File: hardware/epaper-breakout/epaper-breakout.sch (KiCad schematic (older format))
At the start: 94 parts, among them J1 XF2M-3315-1A, J2 C10418, J3 Conn_02x06_Counter_Clockwise, J4 ED060SC4, J5 Conn_01x01_Male, J6 Conn_01x01_Male, J7 Conn_01x10, Q1 AO3401A, Q3 MMBT3904, Q4 MMBT3904, U1 MCP1700-3302E_SOT23, U10 ED060SC7, U11 TP4056, U12 CH340C, U2 PCA9555PW, U3 TPS651851RSLR, U4 XC6206PxxxMR, U5 ESP32-WROVER, U6 ED060XC5

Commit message: re-assign footprints
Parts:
- added C34, C36: 1uF/50V, Capacitor_SMD:C_1206_3216Metric, symbol Device:C
- added C35, C37, C38: 1uF/25V, Capacitor_SMD:C_0805_2012Metric, symbol Device:C
- added R26, R27, R28, R29: 47k, Resistor_SMD:R_0805_2012Metric, symbol Device:R
- added R30: 100k, Resistor_SMD:R_0805_2012Metric, symbol Device:R
- added TP1: VCOM, TestPoint:TestPoint_Pad_2.0x2.0mm, symbol Connector:TestPoint
- C1, C11, C24, C26, C31, C5, C7, C8: footprint Capacitor_SMD:C_0603_1608Metric -> Capacitor_SMD:C_0805_2012Metric; LCSC C19702 -> C1779
- C10, C6: value 47uF -> 22uF; footprint Capacitor_SMD:C_0603_1608Metric -> Capacitor_SMD:C_0805_2012Metric; LCSC C19702 -> C45783
- C12, C32, C9: footprint Capacitor_SMD:C_0603_1608Metric -> Capacitor_SMD:C_0805_2012Metric; LCSC C19702 -> C15850
- C13, C14, C15, C16, C18, C19, C2, C21, C22, C23, C28, C3, C4: footprint Capacitor_SMD:C_0603_1608Metric -> Capacitor_SMD:C_0805_2012Metric
- C20, C25: footprint Capacitor_SMD:C_0603_1608Metric -> Capacitor_SMD:C_0805_2012Metric; LCSC C14858 -> C1710
- C27, C33: footprint Capacitor_SMD:C_0603_1608Metric -> Capacitor_SMD:C_0805_2012Metric; LCSC C19702 -> C49217
- C29, C30: footprint Capacitor_SMD:C_0603_1608Metric -> Capacitor_SMD:C_0805_2012Metric; LCSC C14858 -> C49678
- J4: LCSC C92280 -> C92280/ C262546
- J7: footprint (none) -> Connector_PinHeader_2.54mm:PinHeader_2x05_P2.54mm_Vertical
- L1: footprint Inductor_SMD:L_6.3x6.3_H3 -> Inductor_SMD:L_Taiyo-Yuden_NR-50xx_HandSoldering; LCSC C206321 -> C222947
- L2: footprint Inductor_SMD:L_6.3x6.3_H3 -> Inductor_SMD:L_Taiyo-Yuden_NR-40xx_HandSoldering; LCSC C206321 -> C92959
- R12, R5, R7: footprint (none) -> Resistor_SMD:R_0805_2012Metric; LCSC (none) -> C17477
- R17: value 1M -> 1k; LCSC C17616 -> C17513
- R18: footprint (none) -> Resistor_SMD:R_0805_2012Metric
- R20: LCSC C17593 -> C17740
- R24: LCSC C17593 -> C17713
- TH1: footprint (none) -> Resistor_SMD:R_0603_1608Metric; LCSC (none) -> C71448
- U2: LCSC (none) -> C128392
- U3: footprint RSL48_4P4X4P4 -> tps65185:TPS651851RSLR
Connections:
- net +22V: now also C34.1, R26.1
- net -15V: now also C35.1, R27.1
- net -20V: now also C36.1, R28.1
- net 15V: now also C37.1, R29.1
- net EP_VCOM: now also C38.1, R30.1, TP1.1
- net GND: now also C34.2, C35.2, C36.2, C37.2, C38.2, R26.2, R27.2, R28.2, R29.2, R30.2
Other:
- note added: "Close to EPD connector"
- moved on the sheet: C1, C10, C11, C12, C13, C14, C16, C19, C2, C20, C24, C25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

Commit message: pcb routing
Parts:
- removed J3: Conn_02x06_Counter_Clockwise, Connector_PinHeader_2.54mm:PinHeader_2x06_P2.54mm_Vertical, symbol Connector_Generic:Conn_02x06_Counter_Clockwise
- removed J7: Conn_01x10, Connector_PinHeader_2.54mm:PinHeader_2x05_P2.54mm_Vertical, symbol Connector_Generic:Conn_01x10
- removed R12, R7: 0, Resistor_SMD:R_0805_2012Metric, symbol Device:R
- removed R17: 1k, Resistor_SMD:R_0805_2012Metric, symbol Device:R
- removed U10: ED060SC7, epaper-breakout:AXT334124, symbol epd_breakout:ED060SC7
- added J3: Conn_02x05_Counter_Clockwise, Connector_PinHeader_2.54mm:PinHeader_2x05_P2.54mm_Vertical, symbol Connector_Generic:Conn_02x05_Counter_Clockwise
- added J7: Conn_01x12, Connector_PinHeader_2.54mm:PinHeader_2x06_P2.54mm_Vertical, symbol Connector_Generic:Conn_01x12
- R1, R10, R11, R13, R14, R15, R16, R18, R19, R2, R20, R21, R22, R23, R24, R25, R26, R27, R28, R29, R3, R30, R4, R5, R6, R8, R9: footprint Resistor_SMD:R_0805_2012Metric -> Resistor_SMD:R_0603_1608Metric
- TH1: value 100k -> 10k; LCSC C71448 -> C76589
- TP_VCOM1: renamed from TP1; footprint TestPoint:TestPoint_Pad_2.0x2.0mm -> TestPoint:TestPoint_Pad_D2.0mm
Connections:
- net +3.3V: now also J3.6 (Pin_6), J7.1 (Pin_1)
- net -20V: now also U3.29 (VEE_DIS)
- net A0: now also J3.3 (Pin_3)
- net BAT+: now also R21.1
- net GND: now also U2.2 (A1), U2.3 (A2), J3.5 (Pin_5), J7.2 (Pin_2)
- net IO0: now also J3.7 (Pin_7)
- net MISO: now also J3.10 (Pin_10)
- net MOSI: now also J3.8 (Pin_8)
- net SCL: now also J7.4 (Pin_4)
- net SCLK: now also J3.9 (Pin_9)
- net SDA: now also J7.3 (Pin_3)
- net SENSOR_VN: now also J3.2 (Pin_2)
- net SENSOR_VP: now also J3.1 (Pin_1)
- net SW_VIN: now also J3.4 (Pin_4); no longer R21.1
- net at U2.10 (IO0_6): now also J7.11 (Pin_11)
- net at U2.11 (IO0_7): now also J7.12 (Pin_12)
- net at U2.4 (IO0_0): now also J7.5 (Pin_5)
- net at U2.5 (IO0_1): now also J7.6 (Pin_6)
- net at U2.6 (IO0_2): now also J7.7 (Pin_7)
- net at U2.7 (IO0_3): now also J7.8 (Pin_8)
- net at U2.8 (IO0_4): now also J7.9 (Pin_9)
- net at U2.9 (IO0_5): now also J7.10 (Pin_10)
- no-connect marks 31 -> 27
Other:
- moved on the sheet: C34, C35, C36, C37, C38, J1, J4, R26, R27, R28, R29, R30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

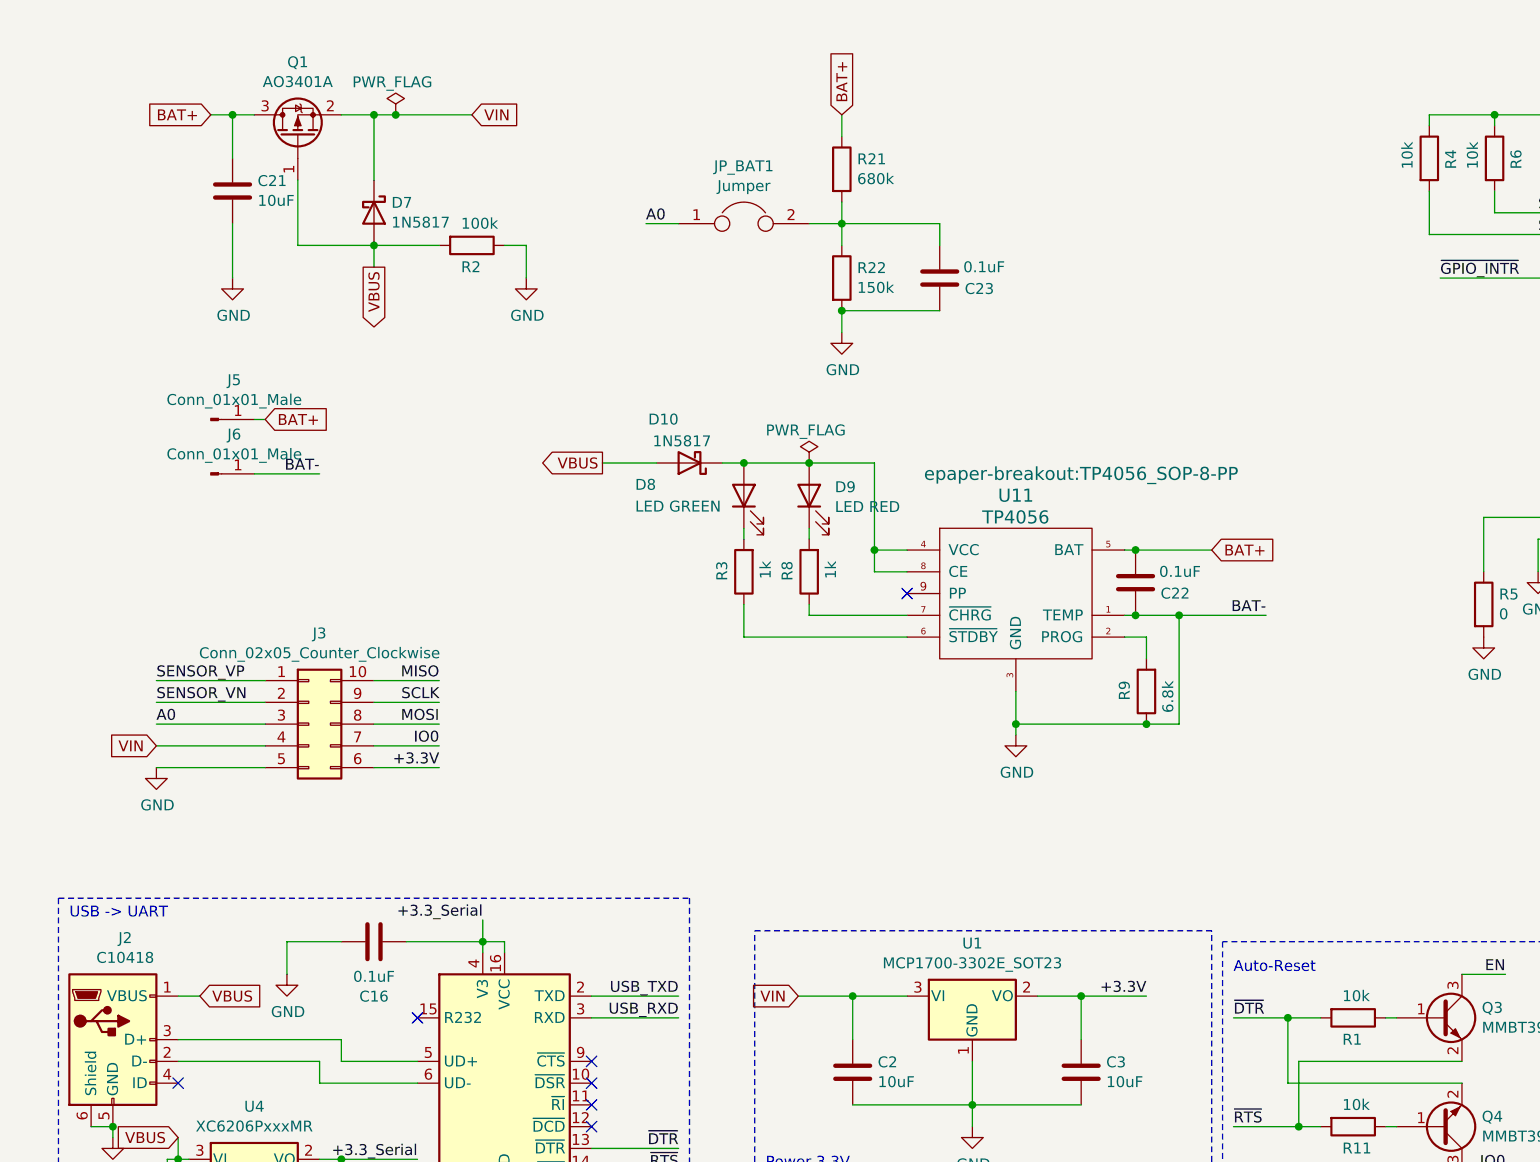
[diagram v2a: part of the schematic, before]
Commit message: add tps2113 for power switchover
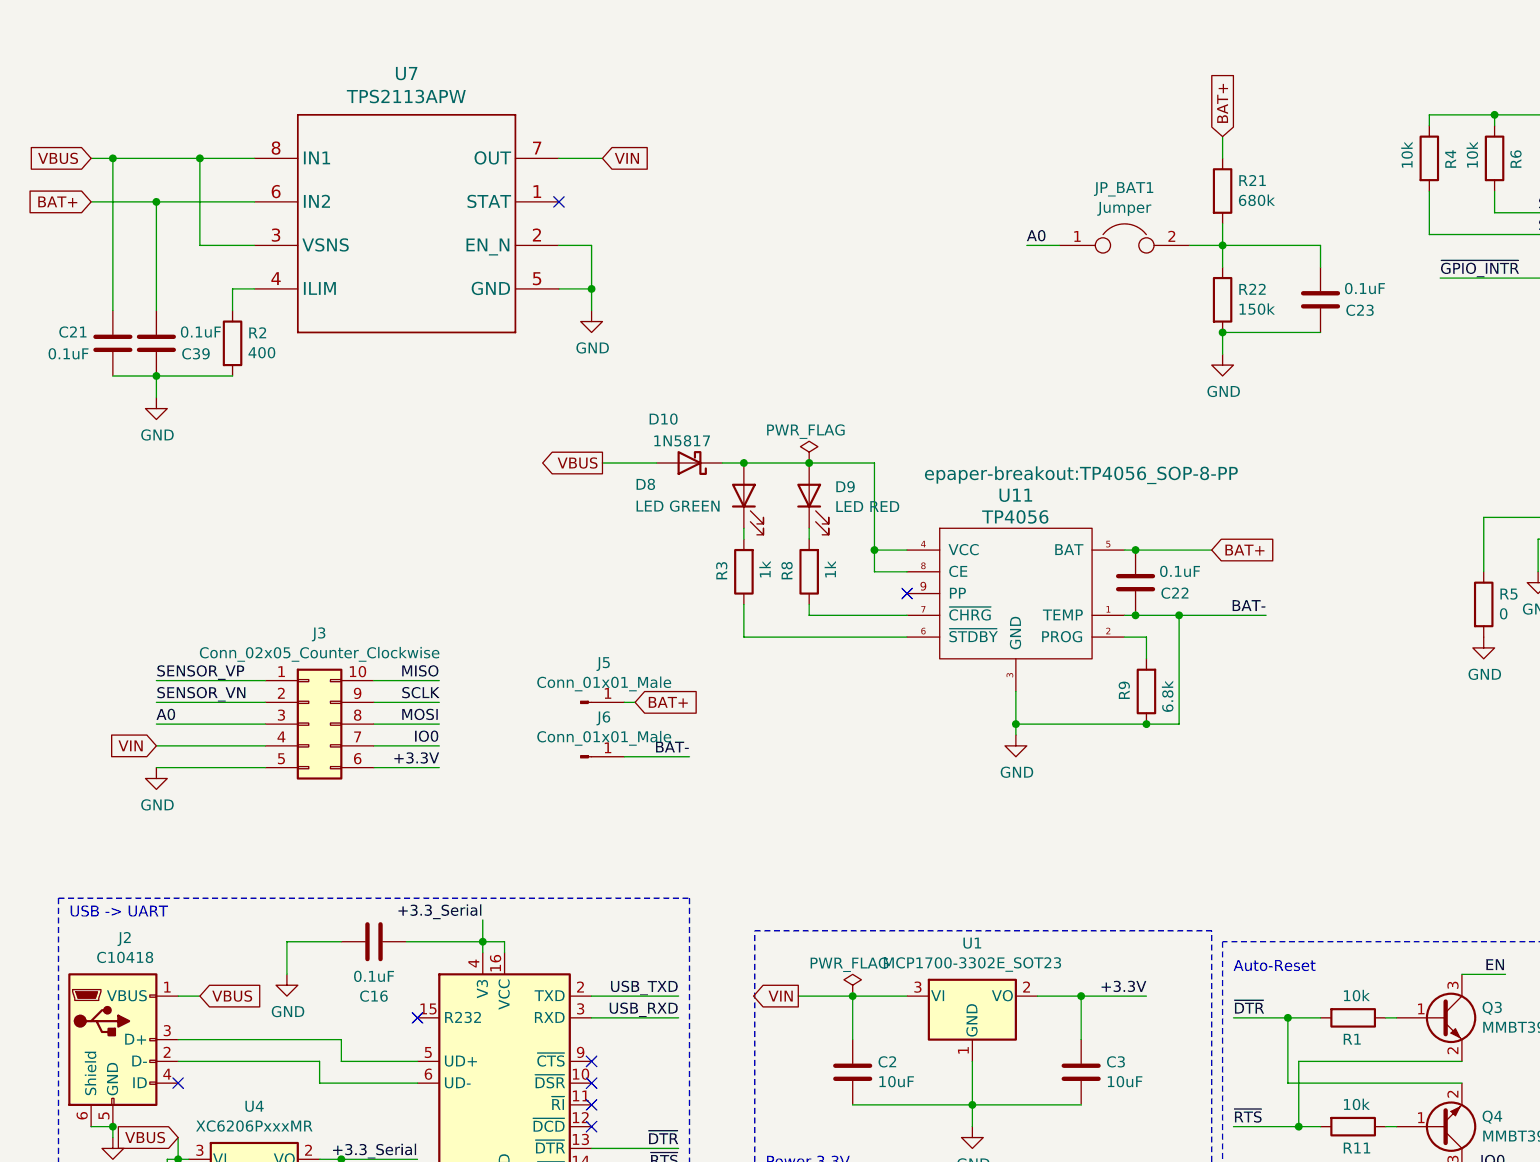
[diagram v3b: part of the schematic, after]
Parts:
- removed D7: 1N5817, Diode_SMD:D_SOD-123, symbol Diode:1N5817
- removed Q1: AO3401A, Package_TO_SOT_SMD:SOT-23, symbol Transistor_FET:AO3401A
- added C39: 0.1uF, Capacitor_SMD:C_0805_2012Metric, symbol Device:C
- added U7: TPS2113APW, epaper-breakout:TPS2113APW, symbol epd_breakout:TPS2113APW
- C21: value 10uF -> 0.1uF; LCSC C19702 -> C14663
- R2: value 100k -> 400; LCSC C17407 -> (none)
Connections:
- net BAT+: now also C39.2, U7.6 (IN2); no longer C21.1
- net GND: now also R2.2, C39.1, U7.2 (EN_N), U7.5 (GND); no longer R2.1
- net SW_VIN: now also U7.7 (OUT)
- net VBUS: now also C21.1, U7.3 (VSNS), U7.8 (IN1); no longer R2.2
- new net: R2.1, U7.4 (ILIM)
- no-connect marks 27 -> 28
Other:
- moved on the sheet: C23, J5, J6, JP_BAT1, R21, R22
